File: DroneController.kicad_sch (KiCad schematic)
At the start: 39 parts, among them J1 Connector, J2 Connector, J3 Connector, P1 USB_C_Plug, SW1 SW_SPDT, U2 W25Q16JVSS, U3 BMP280, U4 MPU-6500, U6 L86-M33, U7 915MHz, U9 AP7361C-33E, Y1 spec

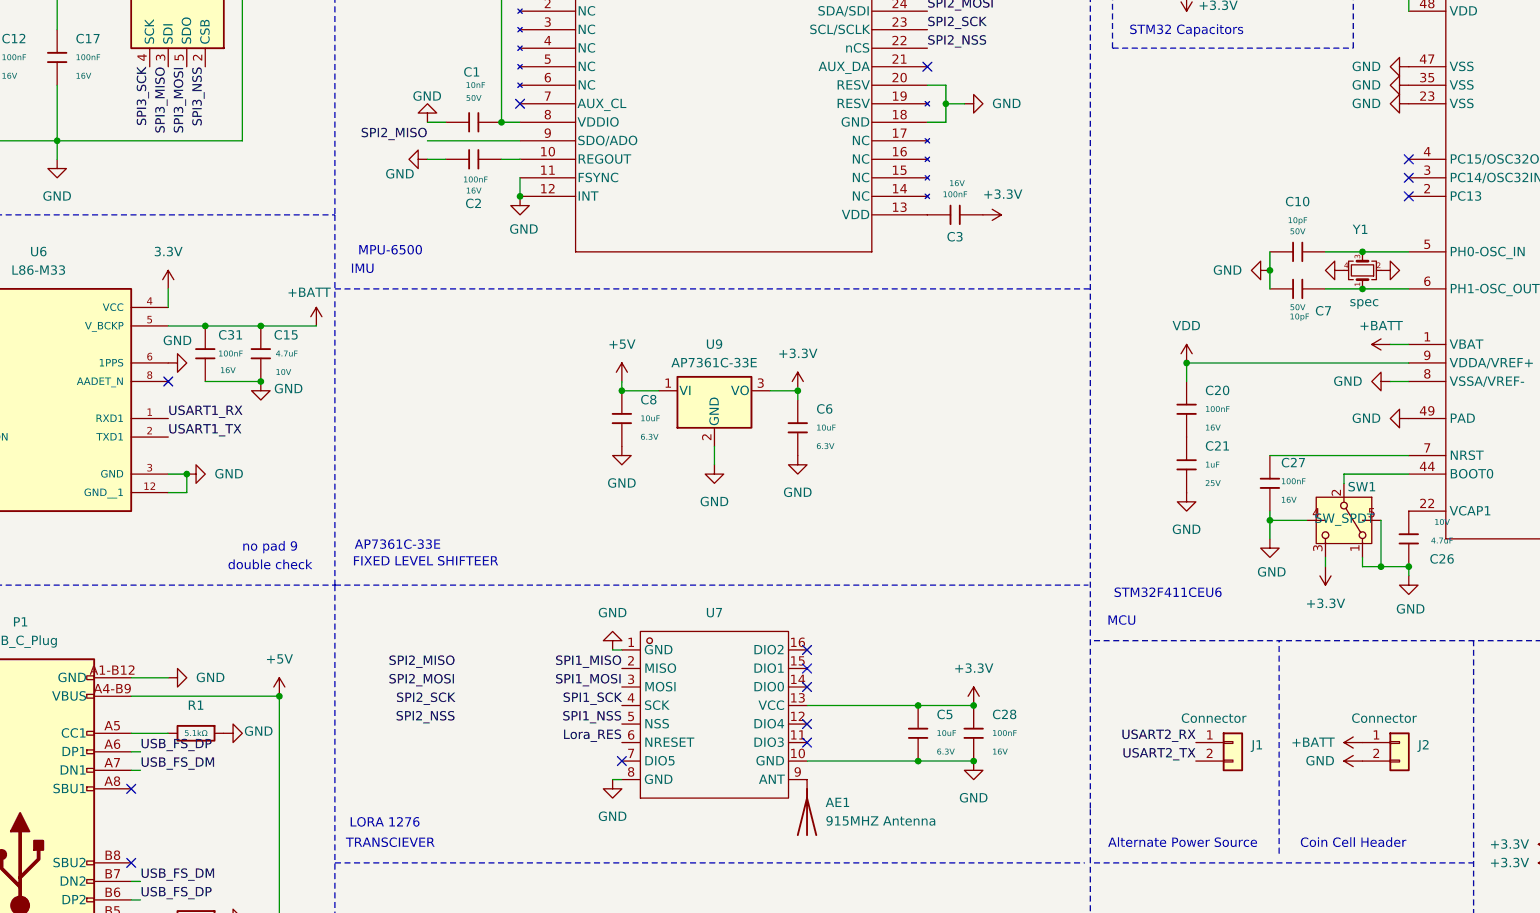
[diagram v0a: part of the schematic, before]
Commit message: Added 3D Models, Changes to Copper Zone, Added Crystal Oscillator to PCB.
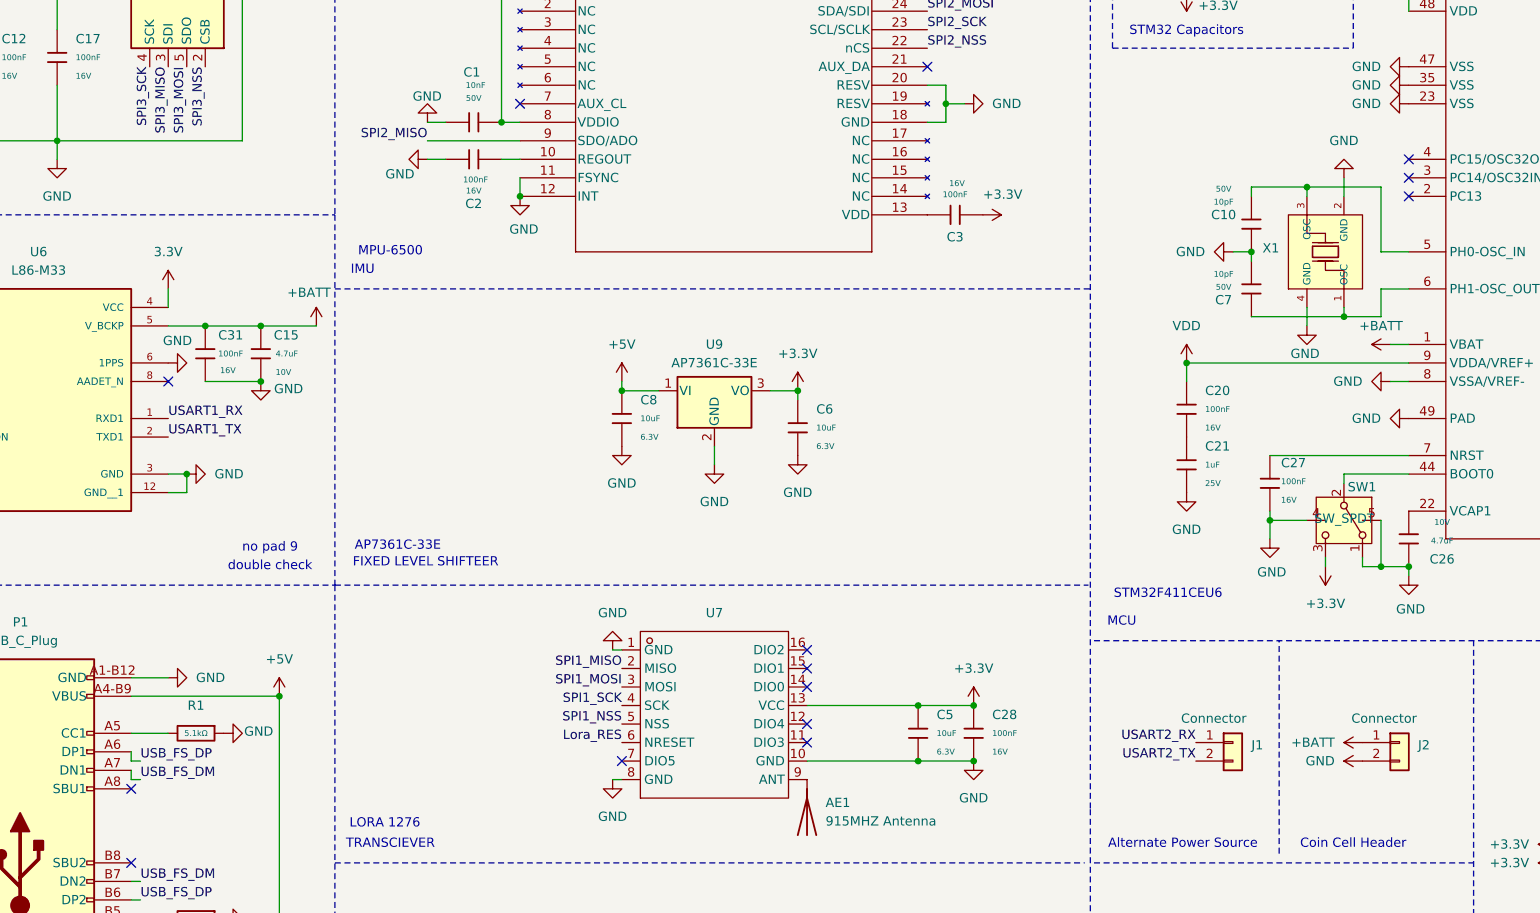
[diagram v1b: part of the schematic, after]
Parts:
- removed Y1: spec, symbol Device:Crystal_GND24_Small
- added X1: X322512MSB4SI, PCM_JLCPCB:CRYSTAL-SMD_4P-L3.2-W2.5-BL, symbol PCM_JLCPCB-Crystals:Crystal, 12MHz, 20pF
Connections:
- net GND: now also X1.2 (GND), X1.4 (GND)
- net at C10.2, U5.5 (PH0-OSC_IN): now also X1.3 (OSC)
- net at C7.1, U5.6 (PH1-OSC_OUT): now also X1.1 (OSC)
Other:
- moved on the sheet: C10, C7

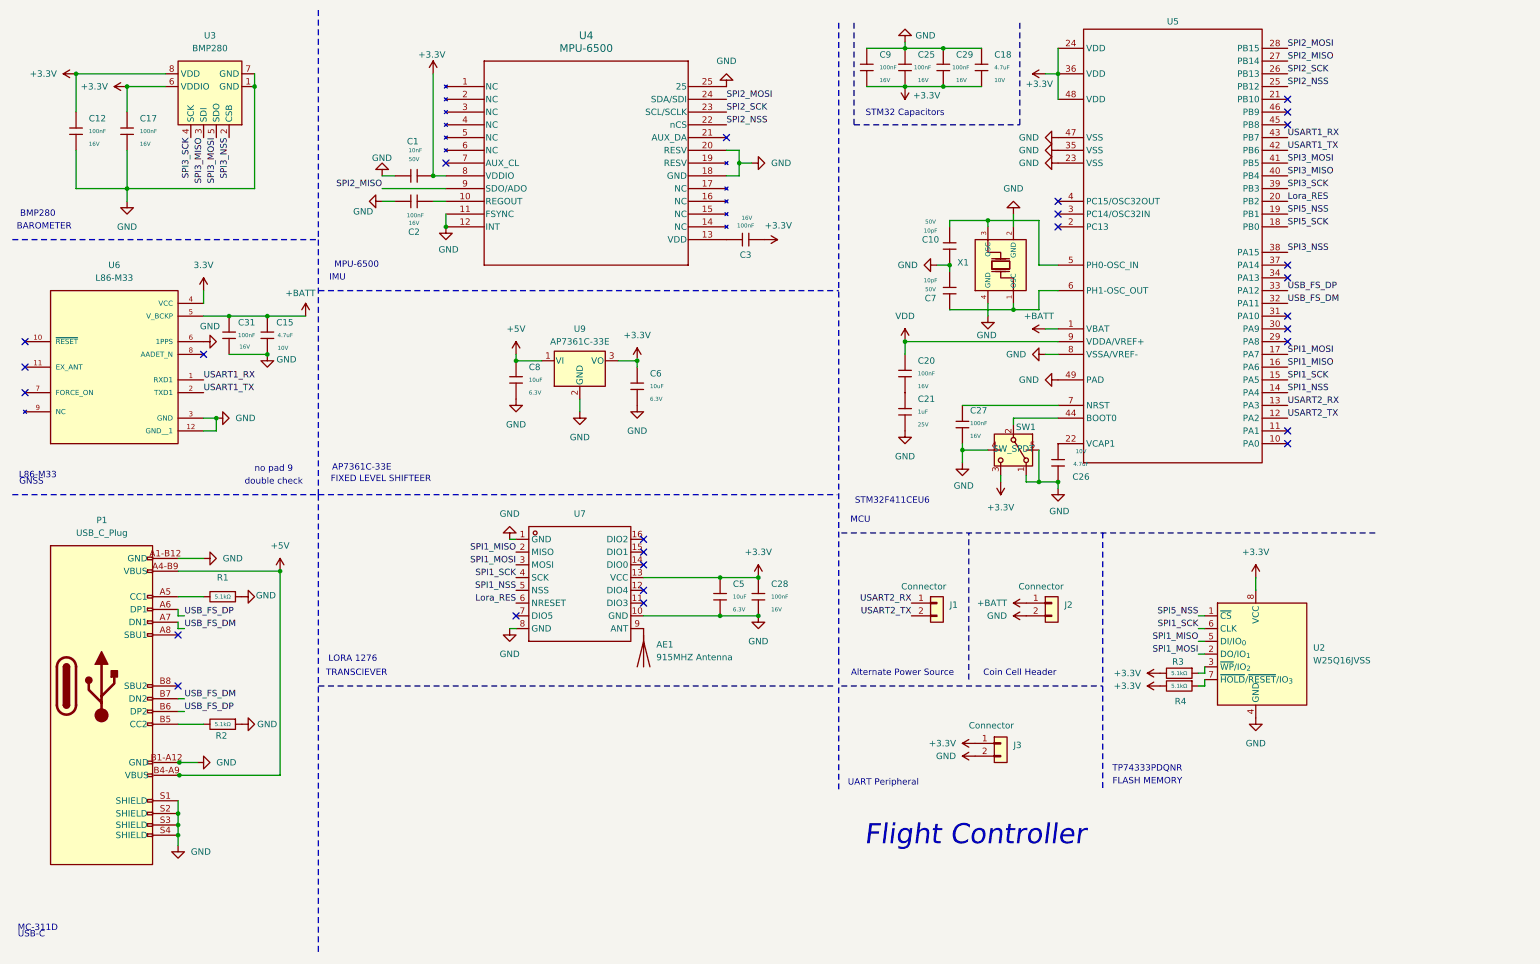
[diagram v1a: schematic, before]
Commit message: Added LCSC Part Numbers
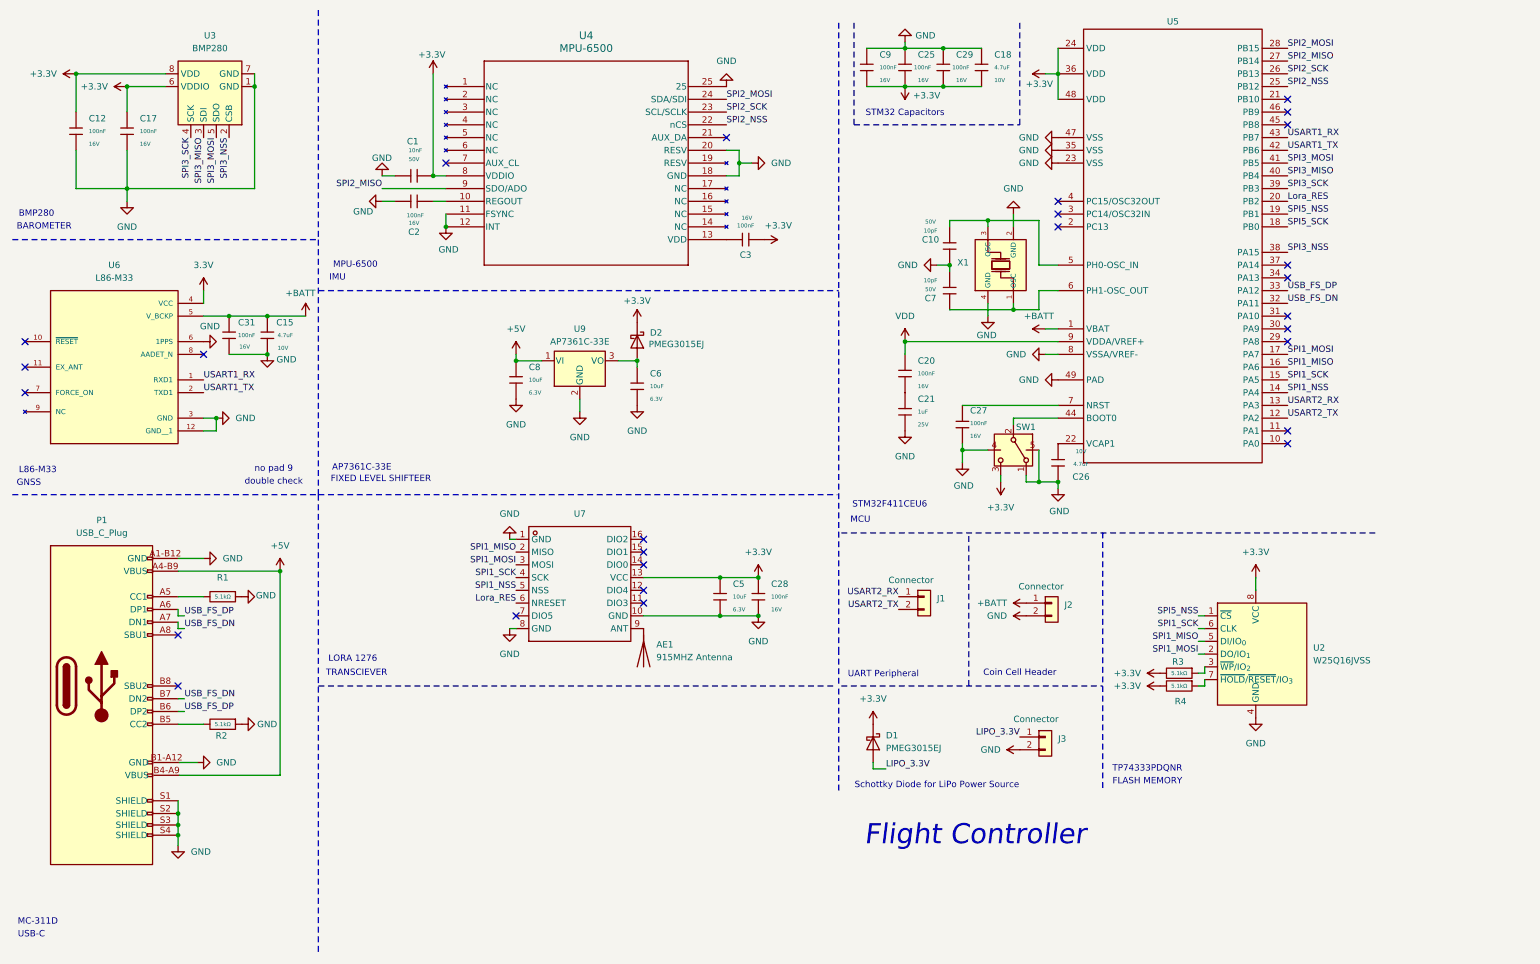
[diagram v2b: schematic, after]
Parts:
- added D1, D2: PMEG3015EJ, Diode_SMD:D_SOD-323F, symbol Diode:PMEG3015EJ
- J1, J2, J3: LCSC (none) -> C5188434
- P1: LCSC (none) -> C136423
- SW1: LCSC (none) -> C2681568
- U2: LCSC (none) -> C131025
- U3: LCSC (none) -> C83291
- U4: LCSC (none) -> C50278
- U5: LCSC (none) -> C60420; Supplier LCSC -> (none); Supplier Part C60420 -> (none)
- U7: LCSC (none) -> C3001531; Supplier LCSC -> (none); Supplier Part C3001531 -> (none)
- U9: LCSC (none) -> C500795
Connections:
- net +3.3V: now also D1.1 (K), D2.1 (K); no longer C6.1, J3.1 (Pin_1), U9.3 (VO)
- net USB_FS_DM renamed USB_FS_DN
- new net: C6.1, D2.2 (A), U9.3 (VO)
- new net LIPO_3.3V: D1.2 (A), J3.1 (Pin_1)
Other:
- note added: "Schottky Diode for LiPo Power Source"
- note removed: "Alternate Power Source"
- moved on the sheet: J1, J3

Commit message: added pull-up resistors, added keepout zones.
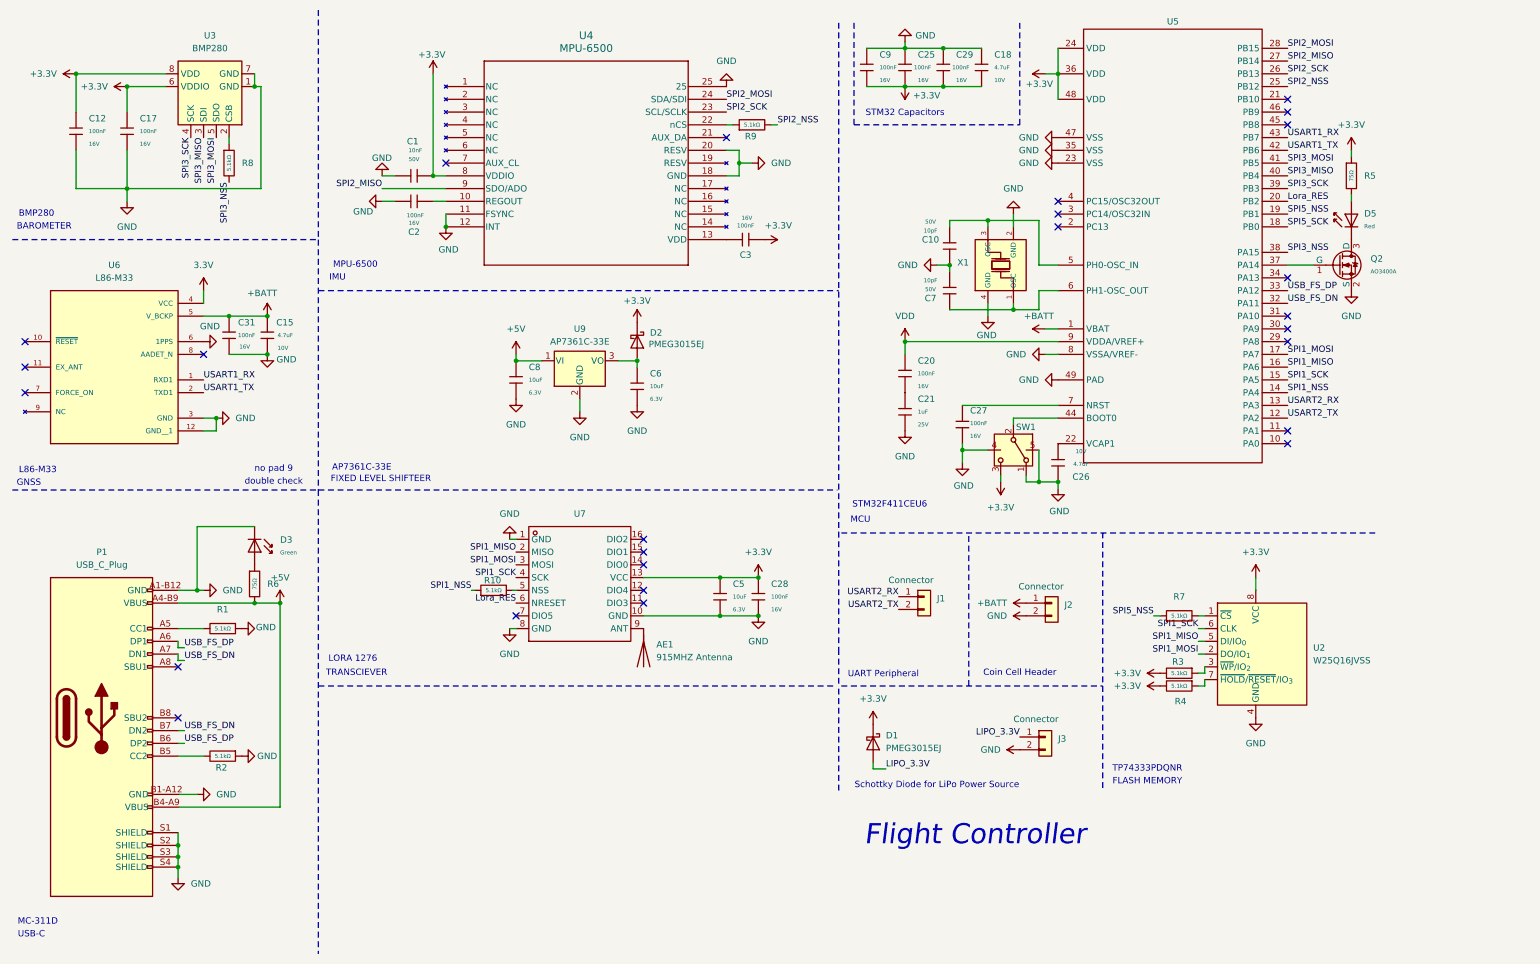
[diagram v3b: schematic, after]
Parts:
- added D3: Green, PCM_JLCPCB:D_0805, symbol PCM_JLCPCB-Diodes:LED,0805,Green
- added D5: Red, PCM_JLCPCB:D_0805, symbol PCM_JLCPCB-Diodes:LED,0805,Red
- added Q2: AO3400A, PCM_JLCPCB:Q_SOT-23, symbol PCM_JLCPCB-Transistors:NMOS,AO3400A
- added R10, R7, R8, R9: 5.1kΩ, PCM_JLCPCB:R_0402, symbol PCM_JLCPCB-Resistors:0402,5.1kΩ
- added R5, R6: 75Ω, PCM_JLCPCB:R_0603, symbol PCM_JLCPCB-Resistors:0603,75Ω
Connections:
- net +3.3V: now also R5.1
- net +5V: now also R6.2
- net GND: now also D3.1, Q2.2 (S)
- net SPI1_NSS: now also R10.1; no longer U7.5 (NSS)
- net SPI2_NSS: now also R9.2; no longer U4.22 (nCS)
- net SPI3_NSS: now also R8.2; no longer U3.2 (CSB)
- net SPI5_NSS: now also R7.1; no longer U2.1 (~{CS})
- net at U5.37 (PA14): now also Q2.1 (G)
- new net: R10.2, U7.5 (NSS)
- new net: R8.1, U3.2 (CSB)
- new net: D3.2, R6.1
- new net: R9.1, U4.22 (nCS)
- new net: R7.2, U2.1 (~{CS})
- new net: D5.1, Q2.3 (D)
- new net: D5.2, R5.2
- no-connect marks 27 -> 26
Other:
- moved on the sheet: P1, R1, R2
